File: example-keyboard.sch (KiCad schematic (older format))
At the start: 11 parts, among them SW1 SW_Push, U1 Elite-C

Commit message: Creates pcb layout
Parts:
- removed R1: 10k, Resistor_THT:R_Box_L14.0mm_W5.0mm_P9.00mm, symbol Device:R_Small
- removed SW_R1_C1, SW_R1_C2, SW_R2_C1, SW_R2_C2: MX, Keebio-Parts:MX-Alps-Choc-1U-NoLED, symbol keebio:MX
- added MX1, MX2, MX3, MX4: SW_R1_C1, Button_Switch_Keyboard:SW_Cherry_MX_1.00u_PCB, symbol Switch:SW_Push
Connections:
- net ROW1: now also MX1.1, MX3.1
- net ROW2: now also MX2.1, MX4.1
- net at D1.2 (A): now also MX1.2
- net at D3.2 (A): now also MX2.2
- net at D2.2 (A): now also MX3.2
- net at D4.2 (A): now also MX4.2
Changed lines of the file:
@@
 $EndComp
-$Comp
-L Device:R_Small R1
-U 1 1 5F96494A
-P 7700 1750
-F 0 "R1" H 7759 1796 50  0000 L CNN
-F 1 "10k" H 7759 1705 50  0000 L CNN
-F 2 "Resistor_THT:R_Box_L14.0mm_W5.0mm_P9.00mm" H 7700 1750 50  0001 C CNN
-F 3 "~" H 7700 1750 50  0001 C CNN
-	1    7700 1750
-	1    0    0    -1
-$EndComp
-$Comp
-L power:+5V #PWR0101
-U 1 1 5F964EFA
-P 7700 1450
-F 0 "#PWR0101" H 7700 1300 50  0001 C CNN
-F 1 "+5V" H 7715 1623 50  0000 C CNN
-F 2 "" H 7700 1450 50  0001 C CNN
-F 3 "" H 7700 1450 50  0001 C CNN
-	1    7700 1450
-	1    0    0    -1
-$EndComp
-Wire Wire Line
-	7350 2100 7700 2100
-Wire Wire Line
-	7700 2100 7700 1850
-Connection ~ 7700 2100
-Wire Wire Line
-	7700 1650 7700 1450
-Wire Wire Line
-	7700 2100 8050 2100
 $Comp
 L power:GND #PWR0102
@@
 	1    7350 2000
 	0    -1   -1   0
-$EndComp
-$Comp
-L keebio:MX SW_R1_C2
-U 1 1 5F969E2E
-P 2800 1500
-F 0 "SW_R1_C2" H 2800 1723 50  0000 C CNN
-F 1 "MX" H 2800 1200 60  0001 C CNN
-F 2 "Keebio-Parts:MX-Alps-Choc-1U-NoLED" H 2800 1500 60  0001 C CNN
-F 3 "" H 2800 1500 60  0001 C CNN
-	1    2800 1500
-	1    0    0    -1
-$EndComp
-$Comp
-L keebio:MX SW_R2_C1
-U 1 1 5F96A74A
-P 1300 2400
-F 0 "SW_R2_C1" H 1300 2623 50  0000 C CNN
-F 1 "MX" H 1300 2100 60  0001 C CNN
-F 2 "Keebio-Parts:MX-Alps-Choc-1U-NoLED" H 1300 2400 60  0001 C CNN
-F 3 "" H 1300 2400 60  0001 C CNN
-	1    1300 2400
-	1    0    0    -1
 $EndComp
 Wire Wire Line
@@
 $EndComp
 $Comp
-L keebio:MX SW_R1_C1
-U 1 1 5F96749A
-P 1300 1500
-F 0 "SW_R1_C1" H 1300 1723 50  0000 C CNN
-F 1 "MX" H 1300 1200 60  0001 C CNN
-F 2 "Keebio-Parts:MX-Alps-Choc-1U-NoLED" H 1300 1500 60  0001 C CNN
-F 3 "" H 1300 1500 60  0001 C CNN
-	1    1300 1500
-	1    0    0    -1
-$EndComp
-$Comp
 L Device:D D3
 U 1 1 5F982F9B
@@
 	0    -1   -1   0
 $EndComp
-$Comp
-L keebio:MX SW_R2_C2
-U 1 1 5F96AD14
-P 2800 2400
-F 0 "SW_R2_C2" H 2800 2623 50  0000 C CNN
-F 1 "MX" H 2800 2100 60  0001 C CNN
-F 2 "Keebio-Parts:MX-Alps-Choc-1U-NoLED" H 2800 2400 60  0001 C CNN
-F 3 "" H 2800 2400 60  0001 C CNN
-	1    2800 2400
-	1    0    0    -1
-$EndComp
-Wire Wire Line
-	1600 1500 1650 1500
 Wire Wire Line
 	1650 1500 1650 1600
@@
 	3150 1900 3500 1900
 Wire Wire Line
-	3100 1500 3150 1500
-Wire Wire Line
 	3150 1500 3150 1600
 Wire Wire Line
@@
 	3150 2800 3500 2800
 Wire Wire Line
-	1600 2400 1650 2400
-Wire Wire Line
 	1650 2400 1650 2500
 Wire Wire Line
-	3100 2400 3150 2400
+	3150 2400 3150 2500
+$Comp
+L Switch:SW_Push MX1
+U 1 1 5F98B4D3
+P 1200 1500
+F 0 "MX1" H 1200 1785 50  0000 C CNN
+F 1 "SW_R1_C1" H 1200 1694 50  0000 C CNN
+F 2 "Button_Switch_Keyboard:SW_Cherry_MX_1.00u_PCB" H 1200 1700 50  0001 C CNN
+F 3 "~" H 1200 1700 50  0001 C CNN
+	1    1200 1500
+	1    0    0    -1
+$EndComp
 Wire Wire Line
-	3150 2400 3150 2500
+	1400 1500 1650 1500
+$Comp
+L Switch:SW_Push MX2
+U 1 1 5F98C447
+P 2700 1500
+F 0 "MX2" H 2700 1785 50  0000 C CNN
+F 1 "SW_R1_C1" H 2700 1694 50  0000 C CNN
+F 2 "Button_Switch_Keyboard:SW_Cherry_MX_1.00u_PCB" H 2700 1700 50  0001 C CNN
+F 3 "~" H 2700 1700 50  0001 C CNN
+	1    2700 1500
+	1    0    0    -1
+$EndComp
+$Comp
+L Switch:SW_Push MX3
+U 1 1 5F98CD21
+P 1200 2400
+F 0 "MX3" H 1200 2685 50  0000 C CNN
+F 1 "SW_R1_C1" H 1200 2594 50  0000 C CNN
+F 2 "Button_Switch_Keyboard:SW_Cherry_MX_1.00u_PCB" H 1200 2600 50  0001 C CNN
+F 3 "~" H 1200 2600 50  0001 C CNN
+	1    1200 2400
+	1    0    0    -1
+$EndComp
+$Comp
+L Switch:SW_Push MX4
+U 1 1 5F98E20A
+P 2700 2400
+F 0 "MX4" H 2700 2685 50  0000 C CNN
+F 1 "SW_R1_C1" H 2700 2594 50  0000 C CNN
+F 2 "Button_Switch_Keyboard:SW_Cherry_MX_1.00u_PCB" H 2700 2600 50  0001 C CNN
+F 3 "~" H 2700 2600 50  0001 C CNN
+	1    2700 2400
+	1    0    0    -1
+$EndComp
+Wire Wire Line
+	1400 2400 1650 2400
+Wire Wire Line
+	2900 2400 3150 2400
+Wire Wire Line
+	2900 1500 3150 1500
+Wire Wire Line
+	7350 2100 8050 2100
 $EndSCHEMATC

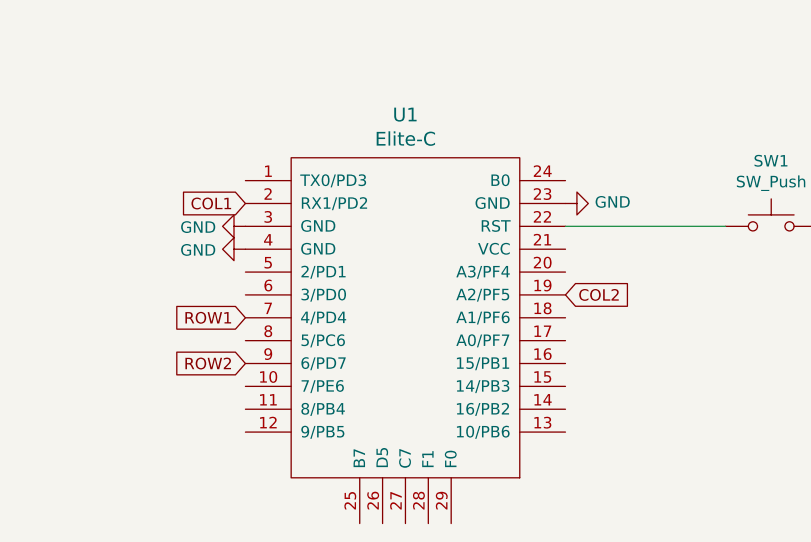
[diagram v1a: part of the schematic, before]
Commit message: Adds routing that I think works but I changed the pins that the rows/columns are talking to so that may bite me
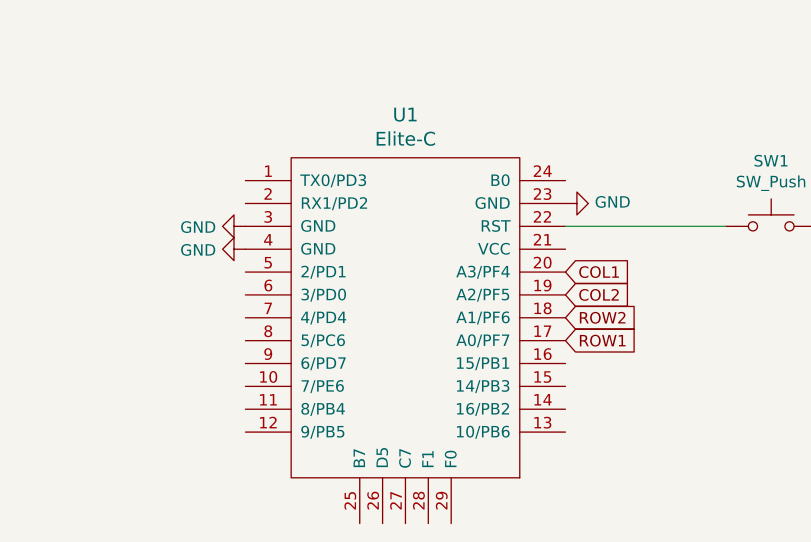
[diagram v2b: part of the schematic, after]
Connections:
- net COL1: now also U1.20 (A3/PF4); no longer U1.2 (RX1/PD2)
- net ROW1: now also U1.17 (A0/PF7); no longer U1.7 (4/PD4)
- net ROW2: now also U1.18 (A1/PF6); no longer U1.9 (6/PD7)
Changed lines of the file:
@@
 $EndDescr
-$Comp
-L keebio:Elite-C U1
-U 1 1 5F9559EF
-P 6650 2450
-F 0 "U1" H 6650 3287 60  0000 C CNN
-F 1 "Elite-C" H 6650 3181 60  0000 C CNN
-F 2 "Keebio-Parts:Elite-C" V 7700 -50 60  0001 C CNN
-F 3 "" V 7700 -50 60  0001 C CNN
-	1    6650 2450
-	1    0    0    -1
-$EndComp
 $Comp
 L Switch:SW_Push SW1
@@
 Text GLabel 3500 2800 2    50   Input ~ 0
 COL2
-Text GLabel 5950 2500 0    50   Input ~ 0
+Text GLabel 7350 2600 2    50   Input ~ 0
 ROW1
-Text GLabel 5950 2700 0    50   Input ~ 0
+Text GLabel 7350 2500 2    50   Input ~ 0
 ROW2
-Text GLabel 5950 2000 0    50   Input ~ 0
-COL1
-Text GLabel 7350 2400 2    50   Input ~ 0
-COL2
 $Comp
 L power:GND #PWR0104
@@
 Wire Wire Line
 	7350 2100 8050 2100
+Text GLabel 7350 2400 2    50   Input ~ 0
+COL2
+Text GLabel 7350 2300 2    50   Input ~ 0
+COL1
+$Comp
+L keebio:Elite-C U1
+U 1 1 5F9559EF
+P 6650 2450
+F 0 "U1" H 6650 3287 60  0000 C CNN
+F 1 "Elite-C" H 6650 3181 60  0000 C CNN
+F 2 "Keebio-Parts:Elite-C" V 7700 -50 60  0001 C CNN
+F 3 "" V 7700 -50 60  0001 C CNN
+	1    6650 2450
+	1    0    0    -1
+$EndComp
 $EndSCHEMATC
